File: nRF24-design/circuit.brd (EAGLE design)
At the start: 40.6 x 49.5 mm, 9 parts, among them IC1 MEGA328-P, J1 AVR_SPI_PROG_3X2PTH, M1 WIRELESS-NRF24L01, Y1 20MHz

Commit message: design: Fix errors (missing power and cipo connections)
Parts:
- added FRAME1: FRAME-LETTER, SparkFun-Aesthetics:CREATIVE_COMMONS
- added J2: (no value), SparkFun-Connectors:2X4
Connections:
- net GND: now also J2.2
- net VCC: now also J2.1
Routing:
- net GND: track 132.4 -> 158.1 mm
- net N$12: track 0.00 -> 15.5 mm
- net VCC: track 120.1 -> 122.4 mm
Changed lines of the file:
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@@
 <setting verticaltext="up"/>
 </settings>
-<grid distance="25" unitdist="mil" unit="mm" style="lines" multiple="1" display="no" altdistance="5" altunitdist="mil" altunit="mil"/>
+<grid distance="25" unitdist="mil" unit="mil" style="lines" multiple="1" display="yes" altdistance="5" altunitdist="mil" altunit="mil"/>
 <layers>
 <layer number="1" name="Top" color="4" fill="1" visible="yes" active="yes"/>
@@
 <attribute name="VALUE" x="41.91" y="35.56" size="0.6096" layer="27" font="vector" ratio="20" rot="R90" align="top-center"/>
 </element>
+<element name="J2" library="SparkFun-Connectors" package="2X4" value="" x="64.135" y="17.145" smashed="yes">
+<attribute name="NAME" x="59.055" y="19.939" size="0.6096" layer="25" font="vector" ratio="20"/>
+<attribute name="VALUE" x="59.055" y="13.462" size="0.6096" layer="27" font="vector" ratio="20"/>
+</element>
+<element name="FRAME1" library="SparkFun-Aesthetics" package="CREATIVE_COMMONS" value="FRAME-LETTER" x="52.705" y="-3.175" smashed="yes">
+<attribute name="DESIGNER" value="Balint Horvath" x="52.705" y="-3.175" size="1.778" layer="27" display="off"/>
+<attribute name="REV" value="2" x="52.705" y="-3.175" size="1.778" layer="27" display="off"/>
+</element>
 </elements>
 <signals>
@@
 <vertex x="33.02" y="12.7"/>
 </polygon>
+<contactref element="J2" pad="2"/>
+<wire x1="68.58" y1="35.56" x2="69.85" y2="34.29" width="0.508" layer="1"/>
+<wire x1="69.85" y1="34.29" x2="69.85" y2="21.59" width="0.508" layer="1"/>
+<wire x1="69.85" y1="21.59" x2="68.58" y2="20.32" width="0.508" layer="1"/>
+<wire x1="68.58" y1="20.32" x2="61.595" y2="20.32" width="0.508" layer="1"/>
+<wire x1="61.595" y1="20.32" x2="60.325" y2="19.05" width="0.508" layer="1"/>
+<wire x1="60.325" y1="19.05" x2="60.325" y2="18.415" width="0.508" layer="1"/>
 </signal>
 <signal name="N$3">
@@
 <wire x1="60.96" y1="40.64" x2="67.31" y2="40.64" width="0.508" layer="16"/>
 <wire x1="50.8" y1="17.78" x2="52.07" y2="16.51" width="0.508" layer="16"/>
-<wire x1="52.07" y1="16.51" x2="62.23" y2="16.51" width="0.508" layer="16"/>
-<wire x1="62.23" y1="16.51" x2="63.5" y2="17.78" width="0.508" layer="16"/>
-<wire x1="63.5" y1="17.78" x2="63.5" y2="26.67" width="0.508" layer="16"/>
+<contactref element="J2" pad="1"/>
+<wire x1="57.15" y1="16.51" x2="57.785" y2="15.875" width="0.508" layer="16"/>
+<wire x1="57.785" y1="15.875" x2="60.325" y2="15.875" width="0.508" layer="16"/>
+<wire x1="52.07" y1="16.51" x2="57.15" y2="16.51" width="0.508" layer="16"/>
+<wire x1="63.5" y1="26.67" x2="63.5" y2="22.86" width="0.508" layer="16"/>
+<wire x1="63.5" y1="22.86" x2="62.23" y2="21.59" width="0.508" layer="16"/>
+<wire x1="62.23" y1="21.59" x2="59.055" y2="21.59" width="0.508" layer="16"/>
+<wire x1="59.055" y1="21.59" x2="58.42" y2="20.955" width="0.508" layer="16"/>
+<wire x1="58.42" y1="19.685" x2="57.15" y2="18.415" width="0.508" layer="16"/>
+<wire x1="57.15" y1="18.415" x2="57.15" y2="16.51" width="0.508" layer="16"/>
+<wire x1="58.42" y1="20.955" x2="58.42" y2="19.685" width="0.508" layer="16"/>
 </signal>
 <signal name="N$9">
@@
 <contactref element="J1" pad="1"/>
 <contactref element="IC1" pad="18"/>
-<wire x1="55.88" y1="29.21" x2="66.04" y2="26.67" width="0" layer="19" extent="1-1"/>
+<wire x1="66.04" y1="26.67" x2="66.04" y2="24.765" width="0.508" layer="1"/>
+<wire x1="66.04" y1="24.765" x2="65.405" y2="24.13" width="0.508" layer="1"/>
+<wire x1="60.96" y1="24.13" x2="59.69" y2="25.4" width="0.508" layer="1"/>
+<wire x1="59.69" y1="27.305" x2="57.785" y2="29.21" width="0.508" layer="1"/>
+<wire x1="57.785" y1="29.21" x2="55.88" y2="29.21" width="0.508" layer="1"/>
+<wire x1="65.405" y1="24.13" x2="60.96" y2="24.13" width="0.508" layer="1"/>
+<wire x1="59.69" y1="25.4" x2="59.69" y2="27.305" width="0.508" layer="1"/>
 </signal>
 <signal name="N$13">

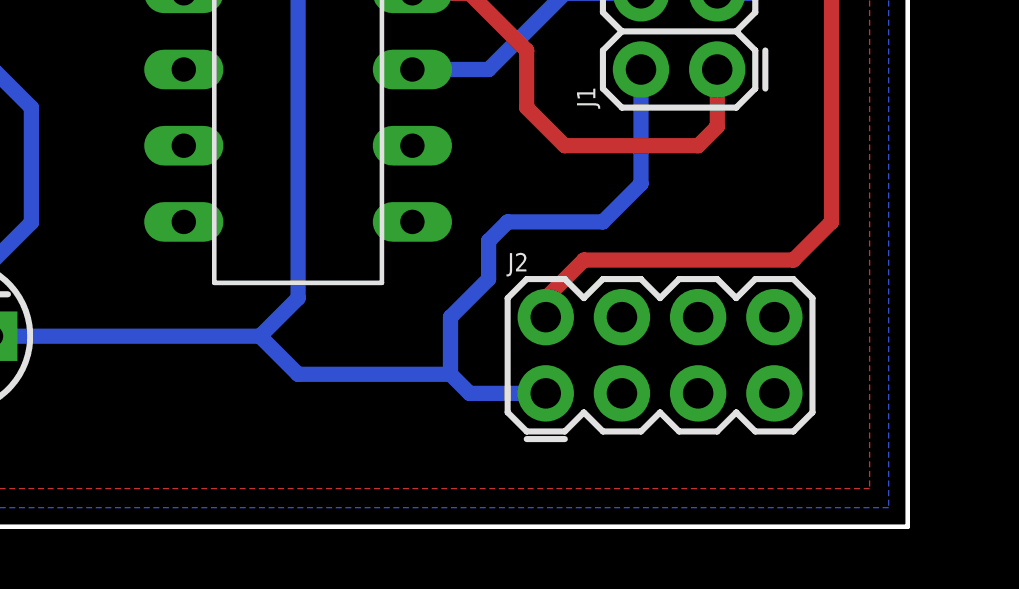
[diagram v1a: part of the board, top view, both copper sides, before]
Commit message: design: add power connectors. Add sensor connectors
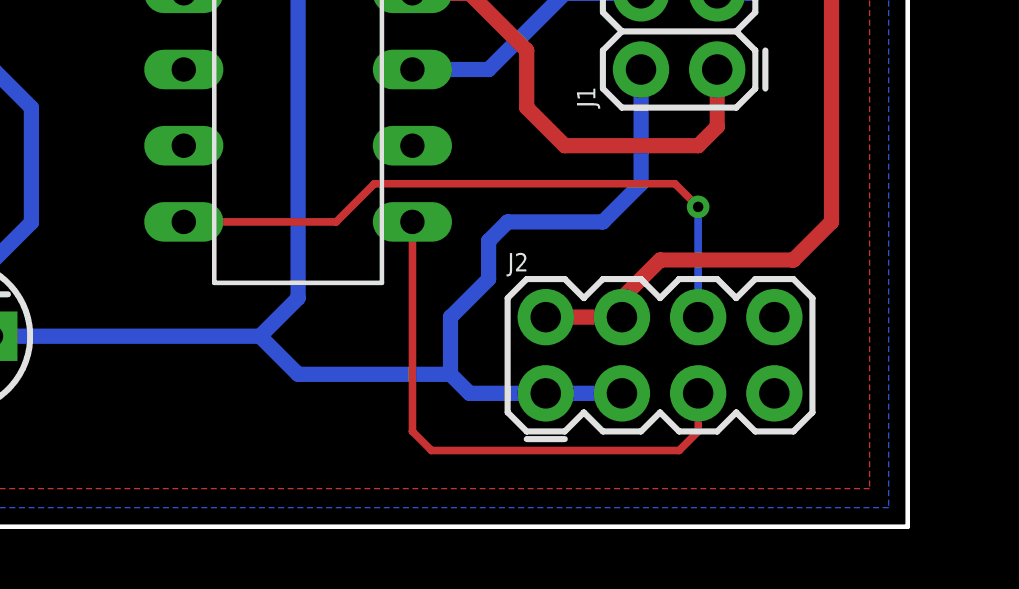
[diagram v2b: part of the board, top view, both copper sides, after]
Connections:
- new net N$15: IC1.15, J2.5
- new net N$17: IC1.14, J2.6
- net GND: now also J2.4
- net VCC: now also J2.3
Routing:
- net N$17: track 0.00 -> 21.7 mm, vias 0 -> 1
- net N$15: track 0.00 -> 18.3 mm
- net VCC: track 122.4 -> 125.0 mm
- net GND: track 158.1 -> 158.8 mm
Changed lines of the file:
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@@
 <element name="FRAME1" library="SparkFun-Aesthetics" package="CREATIVE_COMMONS" value="FRAME-LETTER" x="52.705" y="-3.175" smashed="yes">
 <attribute name="DESIGNER" value="Balint Horvath" x="52.705" y="-3.175" size="1.778" layer="27" display="off"/>
-<attribute name="REV" value="2" x="52.705" y="-3.175" size="1.778" layer="27" display="off"/>
+<attribute name="REV" value="3" x="52.705" y="-3.175" size="1.778" layer="27" display="off"/>
 </element>
 </elements>
@@
 <wire x1="68.58" y1="35.56" x2="69.85" y2="34.29" width="0.508" layer="1"/>
 <wire x1="69.85" y1="34.29" x2="69.85" y2="21.59" width="0.508" layer="1"/>
-<wire x1="69.85" y1="21.59" x2="68.58" y2="20.32" width="0.508" layer="1"/>
-<wire x1="68.58" y1="20.32" x2="61.595" y2="20.32" width="0.508" layer="1"/>
-<wire x1="61.595" y1="20.32" x2="60.325" y2="19.05" width="0.508" layer="1"/>
+<wire x1="68.58" y1="20.32" x2="69.85" y2="21.59" width="0.508" layer="1"/>
 <wire x1="60.325" y1="19.05" x2="60.325" y2="18.415" width="0.508" layer="1"/>
+<contactref element="J2" pad="4"/>
+<wire x1="60.325" y1="18.415" x2="62.865" y2="18.415" width="0.508" layer="1"/>
+<wire x1="62.865" y1="18.415" x2="62.865" y2="19.05" width="0.508" layer="1"/>
+<wire x1="62.865" y1="19.05" x2="64.135" y2="20.32" width="0.508" layer="1"/>
+<wire x1="64.135" y1="20.32" x2="68.58" y2="20.32" width="0.508" layer="1"/>
 </signal>
 <signal name="N$3">
@@
 <wire x1="57.15" y1="18.415" x2="57.15" y2="16.51" width="0.508" layer="16"/>
 <wire x1="58.42" y1="20.955" x2="58.42" y2="19.685" width="0.508" layer="16"/>
+<contactref element="J2" pad="3"/>
+<wire x1="60.325" y1="15.875" x2="62.865" y2="15.875" width="0.508" layer="16"/>
 </signal>
 <signal name="N$9">
@@
 <wire x1="60.96" y1="29.21" x2="63.5" y2="29.21" width="0.508" layer="16"/>
 </signal>
+<signal name="N$15">
+<contactref element="J2" pad="5"/>
+<contactref element="IC1" pad="15"/>
+<wire x1="55.88" y1="21.59" x2="55.88" y2="14.605" width="0.254" layer="1"/>
+<wire x1="55.88" y1="14.605" x2="56.515" y2="13.97" width="0.254" layer="1"/>
+<wire x1="64.77" y1="13.97" x2="65.405" y2="14.605" width="0.254" layer="1"/>
+<wire x1="56.515" y1="13.97" x2="64.77" y2="13.97" width="0.254" layer="1"/>
+<wire x1="65.405" y1="14.605" x2="65.405" y2="15.875" width="0.254" layer="1"/>
+</signal>
+<signal name="N$17">
+<contactref element="IC1" pad="14"/>
+<contactref element="J2" pad="6"/>
+<wire x1="48.26" y1="21.59" x2="53.34" y2="21.59" width="0.254" layer="1"/>
+<wire x1="53.34" y1="21.59" x2="54.61" y2="22.86" width="0.254" layer="1"/>
+<wire x1="54.61" y1="22.86" x2="64.635" y2="22.86" width="0.254" layer="1"/>
+<wire x1="64.635" y1="22.86" x2="65.405" y2="22.09" width="0.254" layer="1"/>
+<via x="65.405" y="22.09" extent="1-16" drill="0.35"/>
+<wire x1="65.405" y1="22.09" x2="65.405" y2="18.415" width="0.254" layer="16"/>
+</signal>
 </signals>

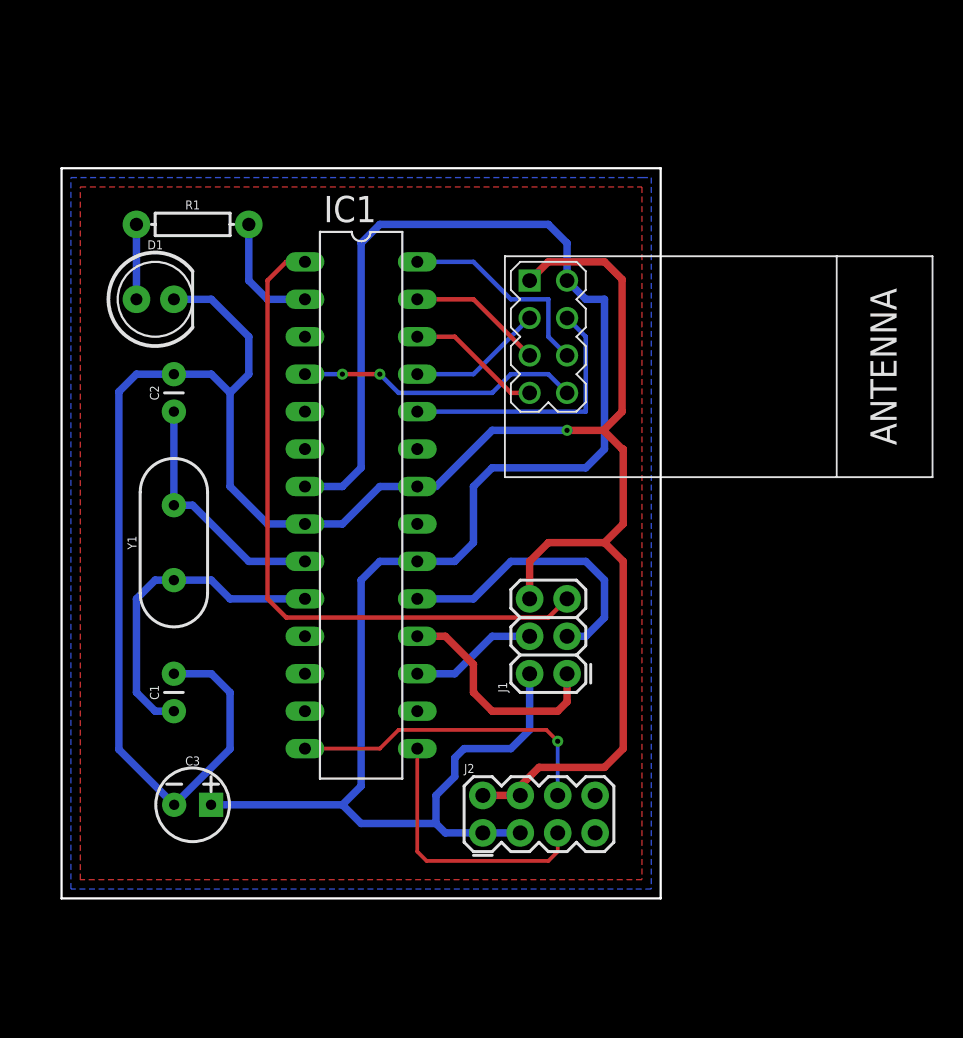
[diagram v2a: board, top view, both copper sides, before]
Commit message: design: Align dimensions to box. Add more decoupling capacitors and labels
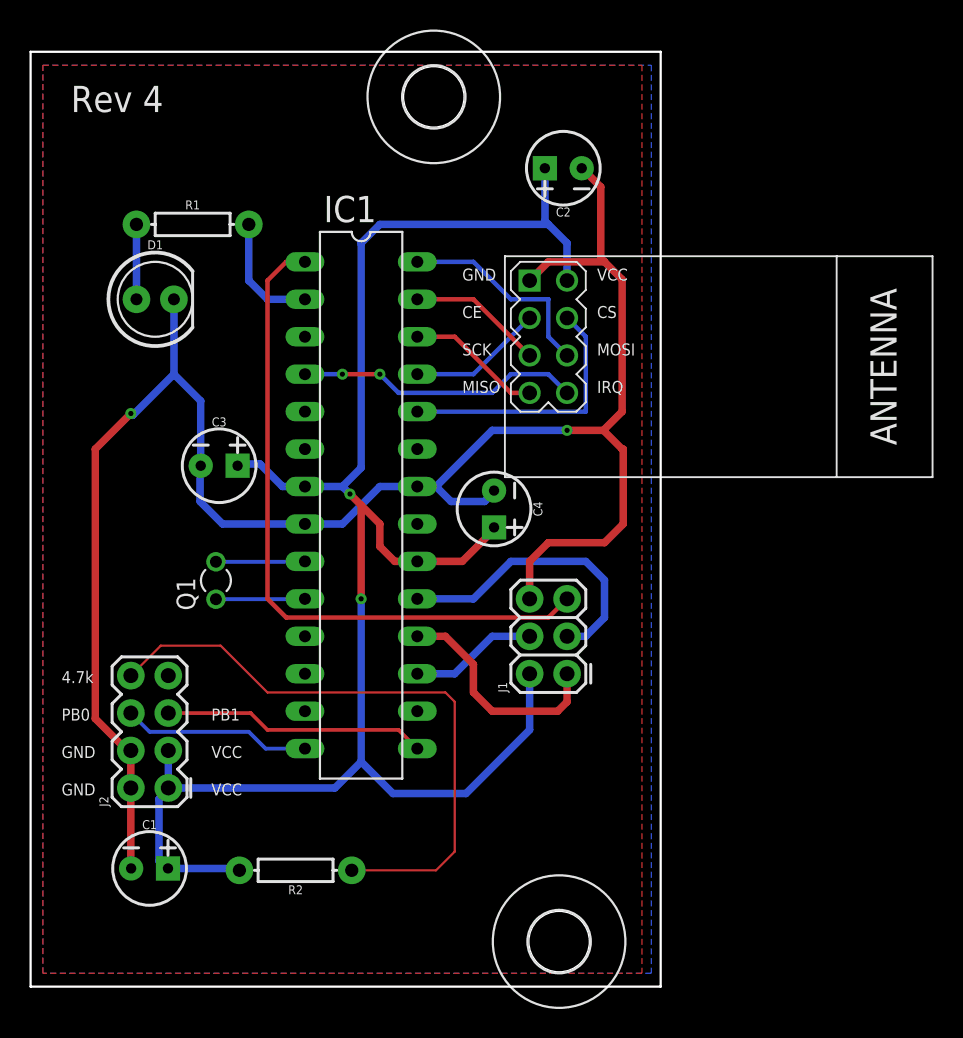
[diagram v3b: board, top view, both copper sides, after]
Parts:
- removed Y1: 20MHz, SparkFun-Clocks:HC49US
- added C4: 0.1uF, SparkFun-Capacitors:CPOL-RADIAL-2.5MM-5MM
- added Q1: 32.768KHz, crystal:TC26V
- added R2: 4.7k, Balint-components:AXIAL-0.3
- added U$1, U$2: (no value), holes:4,1
- C1, C2: value 22pF -> 0.1uF; device SparkFun-Capacitors:CAP-PTH-2.54 -> SparkFun-Capacitors:CPOL-RADIAL-2.5MM-5MM
- J2: value (none) -> ZL262-8DG
- moved C2 30.5 mm to (65.8, 61.0), turned to 180 degrees
- moved J2 27.0 mm to (37.7, 22.7), turned to 90 degrees
- moved C3 23.1 mm to (42.4, 40.8)
- moved FRAME1 17.3 mm to (62.9, -17.1)
- moved C1 12.1 mm to (37.7, 13.5), turned to 0 degrees
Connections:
- new net N$16: J2.8, R2.P$1
- net GND: now also C4.2
- net N$1: now also Q1.2; no longer C2.1, Y1.2
- net N$2: now also Q1.1; no longer C1.1, Y1.1
- net VCC: now also C1.1, C2.1, C4.1, R2.P$2
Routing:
- net N$16: track 0.00 -> 42.1 mm
- net GND: track 158.8 -> 129.4 mm, vias 1 -> 2
- net N$2: track 21.9 -> 6.05 mm
- net N$1: track 16.8 -> 6.05 mm
- net N$17: track 21.7 -> 12.8 mm, vias 1 -> 0
- net VCC: track 125.0 -> 123.3 mm, vias 0 -> 2
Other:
- board size 40.6 x 49.5 mm -> 42.7 x 63.4 mm
- board text added: "4.7k"
- board text added: "CE"
- board text added: "CS"
- board text added: "GND"
- board text added: "IRQ"
- board text added: "MISO"
- board text added: "MOSI"
- board text added: "PB0"
- board text added: "PB1"
- board text added: "Rev 4"
- board text added: "SCK"
- board text added: "VCC"
